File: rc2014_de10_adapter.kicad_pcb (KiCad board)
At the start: 2 copper layers, 101.6 x 50.8 mm, 19 parts, among them J1 Z80 Bus, J2 Pro Bus, J3 Conn_02x20_Odd_Even, J4 M3 Mounting Hole, J5 Conn_01x10_Male, J6 Conn_01x08_Male, U1 SN74LVC245A, U10 MAX40200AUK, U2 SN74LVC245A, U3 SN74LVC245A, U4 SN74LVC245A, U5 AZ1117-3.3, U6 SN74LVC245A, U7 MAX40200AUK, U8 MAX40200AUK, U9 MAX40200AUK

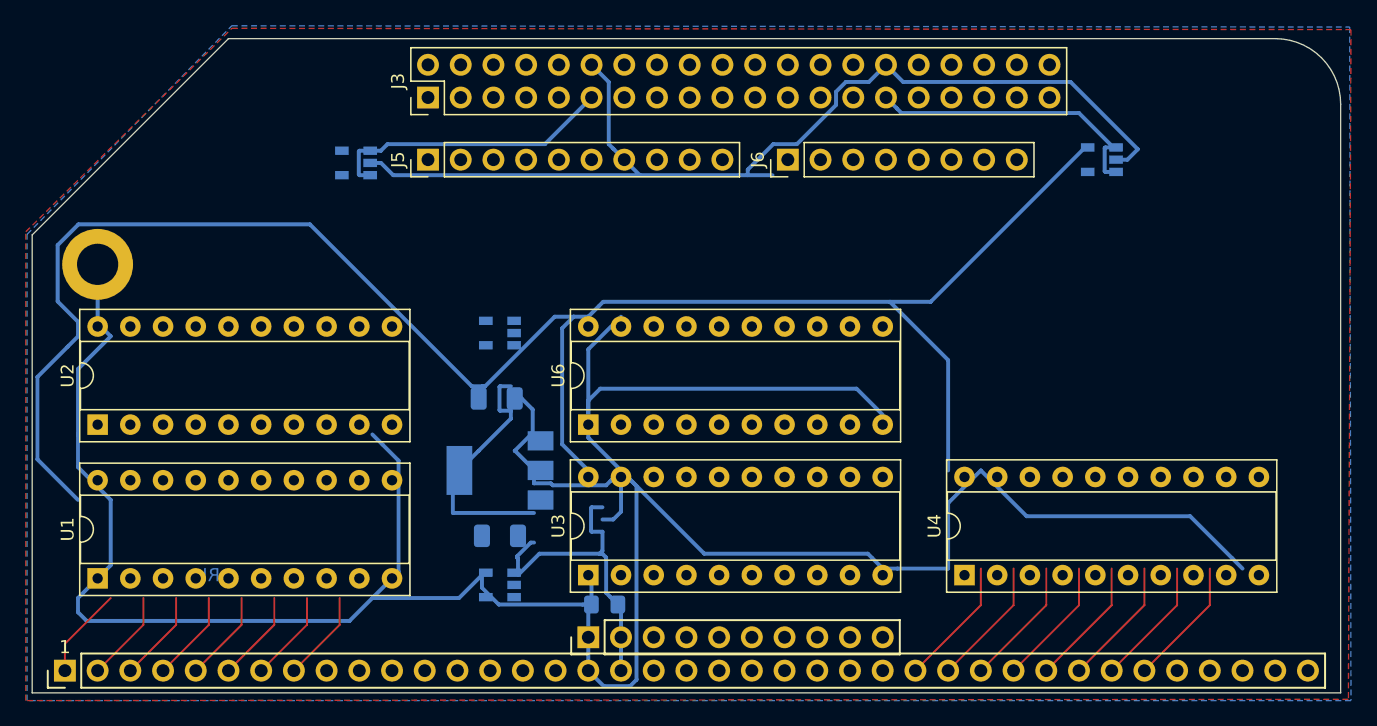
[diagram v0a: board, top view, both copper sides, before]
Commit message: reorganized schematic
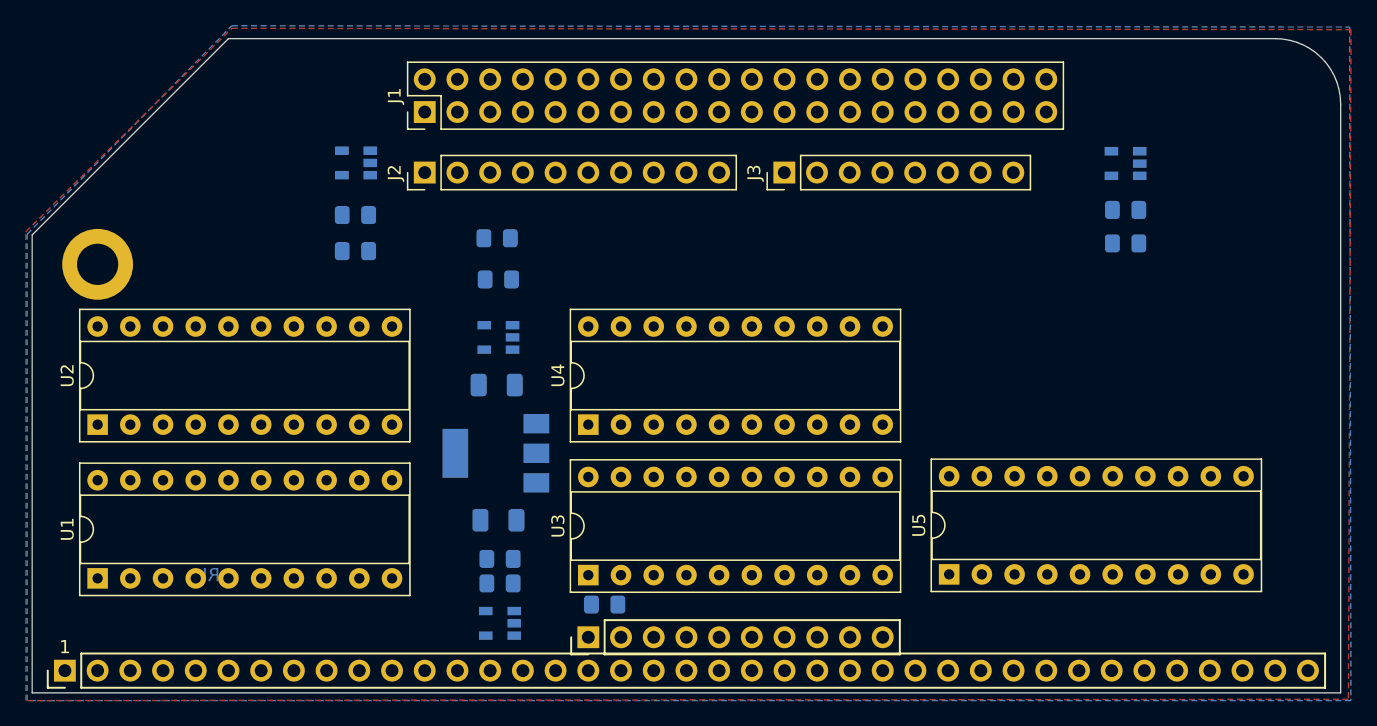
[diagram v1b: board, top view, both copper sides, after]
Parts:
- removed the U7 at (111.8, 99.6)
- removed the U8 at (158.5, 86.1)
- added C10: 1uF, Capacitor_SMD:C_0805_2012Metric_Pad1.15x1.40mm_HandSolder, B.Cu at (160.3, 90.0)
- added C11: 100nF, Capacitor_SMD:C_0805_2012Metric_Pad1.15x1.40mm_HandSolder, B.Cu at (160.3, 92.6)
- added C4: 100nF, Capacitor_SMD:C_0805_2012Metric_Pad1.15x1.40mm_HandSolder, B.Cu at (111.8, 119.0)
- added C5: 1uF, Capacitor_SMD:C_0805_2012Metric_Pad1.15x1.40mm_HandSolder, B.Cu at (111.8, 117.1)
- added C6: 1uF, Capacitor_SMD:C_0805_2012Metric_Pad1.15x1.40mm_HandSolder, B.Cu at (100.5, 93.2)
- added C7: 100nF, Capacitor_SMD:C_0805_2012Metric_Pad1.15x1.40mm_HandSolder, B.Cu at (100.5, 90.4)
- added C8: 100nF, Capacitor_SMD:C_0805_2012Metric_Pad1.15x1.40mm_HandSolder, B.Cu at (111.6, 95.4)
- added C9: 1uF, Capacitor_SMD:C_0805_2012Metric_Pad1.15x1.40mm_HandSolder, B.Cu at (111.5, 92.2)
- added U10: MAX40200AUK, Package_TO_SOT_SMD:SOT-23-5, B.Cu at (160.3, 86.4)
- added U9: MAX40200AUK, Package_TO_SOT_SMD:SOT-23-5, B.Cu at (111.6, 99.9)
- moved U7 2.98 mm to (111.8, 122.1)
- moved U6 1.37 mm to (111.4, 108.9)
- moved C2 1.21 mm to (111.6, 114.1)
- moved U5 1.19 mm to (146.6, 118.3)
- moved J1 1.16 mm to (105.9, 82.4)
- moved C3 1.04 mm to (111.5, 103.6)
- moved J3 1.04 mm to (133.8, 87.1)
- moved J2 1.03 mm to (105.9, 87.1)
- renumbered J3 to J1, J5 to J2, J6 to J3, J1 to J5, J2 to J6, U6 to U4, U4 to U5, U5 to U6, U9 to U7, U10 to U8
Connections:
- J2 pad 9: (no net) -> PAGEF
- J3 pad 1: (no net) -> RxF
- J3 pad 2: (no net) -> TxF
- J3 pad 8: (no net) -> DIR
- J5 pad 35: (no net) -> Tx
- J5 pad 36: (no net) -> Rx
- J6 pad 4: (no net) -> PAGE
- U1 pad 1: GND -> +3V3
- U2 pad 1: GND -> +3V3
- U3 pad 1: GND -> +3V3
- U3 pad 11: (no net) -> TxF
- U3 pad 9: (no net) -> Tx
- U4 pad 11: (no net) -> RxF
- U4 pad 12: (no net) -> PAGEF
- U4 pad 8: (no net) -> PAGE
- U4 pad 9: (no net) -> Rx
- U5 pad 1: GND -> DIR
- U7 pad 5: +5V -> 5V
- U8 pad 5: +5V -> 5V
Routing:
- net GND: track 320.2 -> 0.00 mm
- net +3V3: track 144.7 -> 0.00 mm
- net 5V: track 25.6 -> 0.00 mm
- net 3V3F: track 23.1 -> 0.00 mm
- net 5VF: track 22.5 -> 0.00 mm
- net 3V3: track 19.7 -> 0.00 mm
- net D5: track 10.0 -> 0.00 mm
- net D4: track 10.0 -> 0.00 mm
- net D1: track 10.0 -> 0.00 mm
- net D0: track 10.0 -> 0.00 mm
- net D7: track 10.0 -> 0.00 mm
- net D6: track 10.0 -> 0.00 mm
- net D3: track 10.0 -> 0.00 mm
- net D2: track 10.0 -> 0.00 mm
- net A15: track 7.11 -> 0.00 mm
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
